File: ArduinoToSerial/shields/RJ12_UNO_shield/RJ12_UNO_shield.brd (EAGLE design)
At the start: 69 x 57 mm, 15 parts, among them CON1 RJ12, CON2 RJ12, CON3 RJ12, CON4 RJ12

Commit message: increased isolate space from GND plate. Fixed RX-TX connection
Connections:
- net N$15: now also U$5.TX; no longer U$5.RX
- net N$16: now also U$5.RX; no longer U$5.TX
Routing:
- net N$16: track 53.3 -> 49.3 mm
- net N$15: track 51.1 -> 52.9 mm
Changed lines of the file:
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@@
 <signal name="N$15">
 <contactref element="D0-D7" pad="D0"/>
-<contactref element="U$5" pad="RX"/>
 <contactref element="D0-D1" pad="D0"/>
-<wire x1="32.2" y1="36.4" x2="32.2" y2="37.8" width="0.35" layer="1"/>
-<wire x1="64.75" y1="3.85" x2="32.2" y2="36.4" width="0.35" layer="1"/>
-<wire x1="32.2" y1="37.8" x2="32.05" y2="38" width="0.35" layer="1"/>
-<wire x1="64.75" y1="3.85" x2="64.96" y2="3.81" width="0.35" layer="1"/>
 <wire x1="64.96" y1="3.81" x2="68.2" y2="3.81" width="0.35" layer="1"/>
+<contactref element="U$5" pad="TX"/>
+<wire x1="64.96" y1="3.81" x2="63.7" y2="3.81" width="0.35" layer="1"/>
+<wire x1="63.7" y1="3.81" x2="29.51" y2="38" width="0.35" layer="1"/>
 </signal>
 <signal name="N$16">
 <contactref element="D0-D7" pad="D1"/>
-<contactref element="U$5" pad="TX"/>
-<wire x1="65.1076" y1="6.4008" x2="64.96" y2="6.35" width="0.35" layer="1"/>
 <contactref element="D0-D1" pad="D1"/>
-<wire x1="30.45" y1="38.15" x2="29.75" y2="38.15" width="0.35" layer="1"/>
-<wire x1="31.5" y1="39.2" x2="30.45" y2="38.15" width="0.35" layer="1"/>
-<wire x1="32.55" y1="39.2" x2="31.5" y2="39.2" width="0.35" layer="1"/>
-<wire x1="29.75" y1="38.15" x2="29.51" y2="38" width="0.35" layer="1"/>
-<wire x1="65.1" y1="6.65" x2="64.96" y2="6.35" width="0.35" layer="1"/>
-<wire x1="65.1" y1="6.65" x2="32.55" y2="39.2" width="0.35" layer="1"/>
 <wire x1="68.2" y1="6.35" x2="64.96" y2="6.35" width="0.35" layer="1"/>
+<contactref element="U$5" pad="RX"/>
+<wire x1="64.96" y1="6.35" x2="63.7" y2="6.35" width="0.35" layer="1"/>
+<wire x1="63.7" y1="6.35" x2="32.05" y2="38" width="0.35" layer="1"/>
 </signal>
 <signal name="N$18">
@@
 <wire x1="10.85" y1="47.6" x2="10.85" y2="46.9" width="0.35" layer="1"/>
 <wire x1="11.8" y1="48.55" x2="10.85" y2="47.6" width="0.35" layer="1"/>
-<wire x1="11.8" y1="51" x2="11.8" y2="48.55" width="0.35" layer="1"/>
-<wire x1="12.6" y1="51.8" x2="11.8" y2="51" width="0.35" layer="1"/>
-<wire x1="36.5" y1="51.8" x2="12.6" y2="51.8" width="0.35" layer="1"/>
+<wire x1="11.8" y1="51.1" x2="11.8" y2="48.55" width="0.35" layer="1"/>
+<wire x1="12.5" y1="51.8" x2="11.8" y2="51.1" width="0.35" layer="1"/>
+<wire x1="36.5" y1="51.8" x2="12.5" y2="51.8" width="0.35" layer="1"/>
 <wire x1="60.3" y1="28" x2="36.5" y2="51.8" width="0.35" layer="1"/>
 <wire x1="64.75" y1="28" x2="60.3" y2="28" width="0.35" layer="1"/>
@@
 <contactref element="U$5" pad="GND"/>
 <contactref element="POWER" pad="GND(1)"/>
-<polygon width="0.35" layer="1">
+<polygon width="0.35" layer="1" isolate="0.4064">
 <vertex x="1.2" y="56.8"/>
-<vertex x="1.1" y="0.2"/>
+<vertex x="1.2" y="0.2"/>
 <vertex x="69.8" y="0.2"/>
-<vertex x="69.9" y="56.8"/>
-</polygon>
-<polygon width="0.35" layer="16">
+<vertex x="69.8" y="56.8"/>
+</polygon>
+<polygon width="0.35" layer="16" isolate="0.4064">
 <vertex x="1.2" y="56.8"/>
-<vertex x="1.1" y="0.2"/>
+<vertex x="1.2" y="0.2"/>
 <vertex x="69.8" y="0.2"/>
-<vertex x="69.9" y="56.8"/>
+<vertex x="69.8" y="56.8"/>
 </polygon>
 <contactref element="POWER1" pad="GBD(2)"/>
@@
 <vertex x="8.3" y="5.2"/>
 <vertex x="8.3" y="10.6"/>
+</polygon>
+<polygon width="0.35" layer="1" orphans="yes">
+<vertex x="2.2" y="24.4"/>
+<vertex x="2.2" y="19"/>
+<vertex x="7.9" y="18.9"/>
+<vertex x="7.9" y="24.3"/>
+</polygon>
+<polygon width="0.35" layer="1" orphans="yes">
+<vertex x="2.4" y="37.8"/>
+<vertex x="2.4" y="32.4"/>
+<vertex x="8.1" y="32.3"/>
+<vertex x="8.1" y="37.7"/>
+</polygon>
+<polygon width="0.35" layer="1" orphans="yes">
+<vertex x="2.3" y="51.4"/>
+<vertex x="2.3" y="46"/>
+<vertex x="8" y="45.9"/>
+<vertex x="8" y="51.3"/>
 </polygon>
 </signal>
@@
 <wire x1="68.2" y1="16.51" x2="64.96" y2="16.51" width="0.35" layer="1"/>
 </signal>
+<signal name="N$10">
+</signal>
 </signals>

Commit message: added a THT resistor version
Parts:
- removed R1, R2: (no value), resistor:R0805
- added R1-A, R2-A: (no value), resistor:0207/10
- added R1-B, R2-B: (no value), resistor:R0805W
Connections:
- net N$1: now also R1-A.1, R1-B.1; no longer R1.1
- net N$2: now also R2-A.1, R2-B.1; no longer R2.1
- net N$31: now also R1-A.2, R1-B.2, R2-A.2, R2-B.2; no longer R1.2, R2.2
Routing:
- net N$31: track 53.1 -> 75.4 mm
- net N$2: track 57.4 -> 60.2 mm
- net N$1: track 67.7 -> 67.0 mm

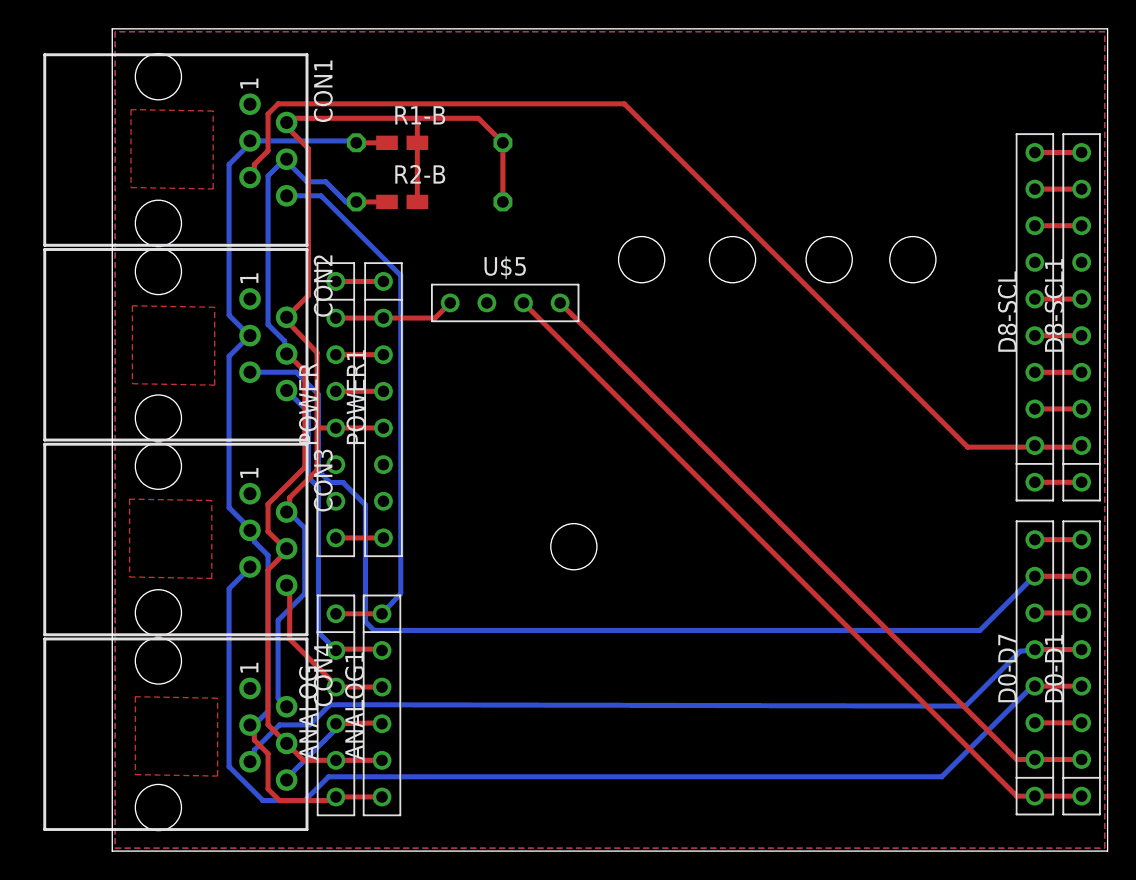
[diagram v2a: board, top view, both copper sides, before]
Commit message: added THT + SMD resistor
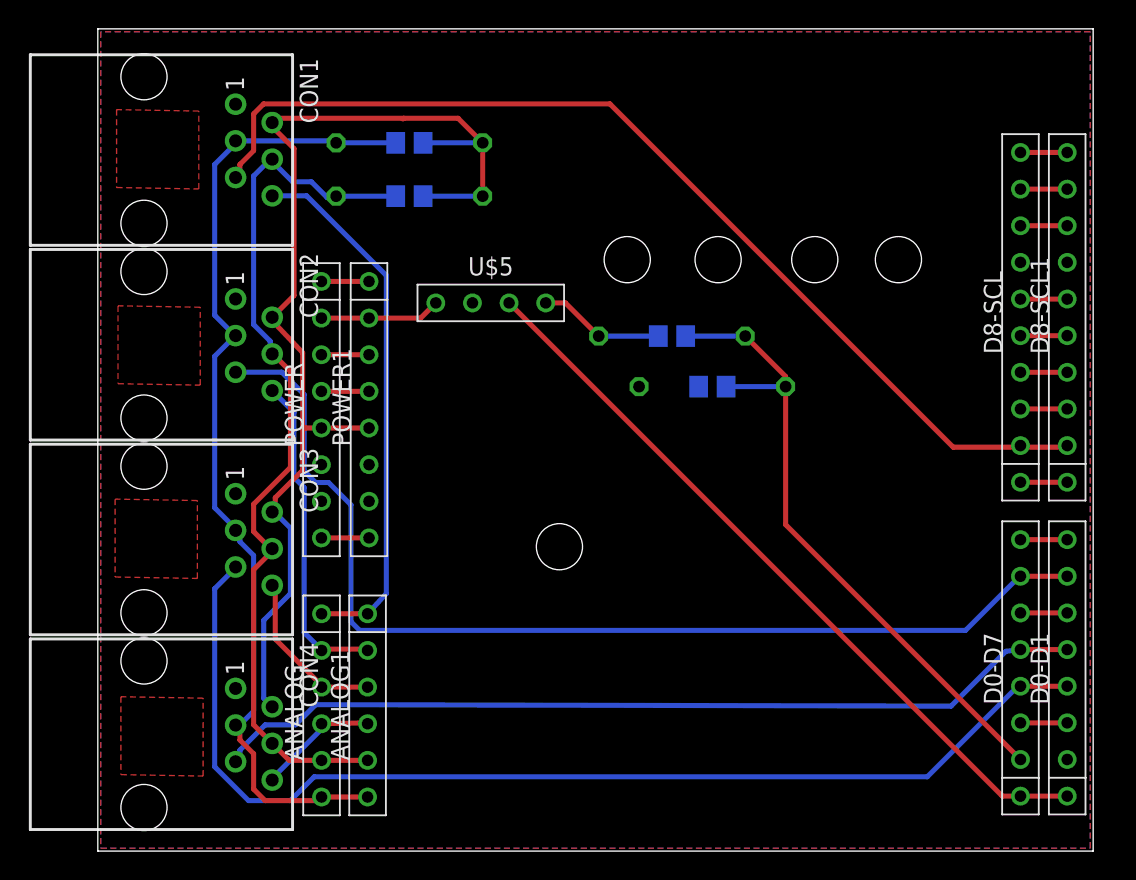
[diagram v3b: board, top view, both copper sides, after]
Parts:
- removed R1-A, R2-A: (no value), resistor:0207/10
- removed R1-B, R2-B: (no value), resistor:R0805W
- added R1, R2, U$1, U$2: R_THT_SMD, AtoG:R_THT_SMD
- moved ANALOG 1.00 mm to (15.5, 10.1)
- moved ANALOG1 1.00 mm to (18.7, 10.1)
- moved CON1 1.00 mm to (3.20, 48.6)
- moved CON2 1.00 mm to (3.20, 35.1)
- moved CON3 1.00 mm to (3.20, 21.6)
- moved CON4 1.00 mm to (3.20, 8.10)
- moved D0-D1 1.00 mm to (67.2, 12.7)
- moved D8-SCL1 1.00 mm to (67.2, 37.0)
- moved POWER 1.00 mm to (15.5, 30.6)
- moved POWER1 1.00 mm to (18.8, 30.6)
- moved U$5 1.00 mm to (27.2, 38.0)
- moved D0-D7 1.00 mm to (64.0, 12.7)
- moved D8-SCL 1.00 mm to (64.0, 37.0)
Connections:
- new net N$21: D0-D1.D1, D0-D7.D1, U$1.2A, U$1.2B, U$2.2A, U$2.2B
- net GND: now also U$2.1A, U$2.1B
- net N$1: now also R1.1A, R1.1B; no longer R1-A.1, R1-B.1
- net N$16: now also U$1.1A, U$1.1B; no longer D0-D1.D1, D0-D7.D1
- net N$2: now also R2.1A, R2.1B; no longer R2-A.1, R2-B.1
- net N$31: now also R1.2A, R1.2B, R2.2A, R2.2B; no longer R1-A.2, R1-B.2, R2-A.2, R2-B.2
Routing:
- net N$21: track 0.00 -> 45.5 mm
- net N$16: track 49.3 -> 8.75 mm
- net N$31: track 75.4 -> 77.1 mm
- net N$1: track 67.0 -> 68.6 mm
- net N$2: track 60.2 -> 61.7 mm
